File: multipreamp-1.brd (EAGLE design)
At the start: 100 x 50 mm, 138 parts, among them Q1 J201, Q2 J201, Q3 J201, Q4 J201, Q5 J201, Q6 J201, Q7 J201, Q8 2N5088

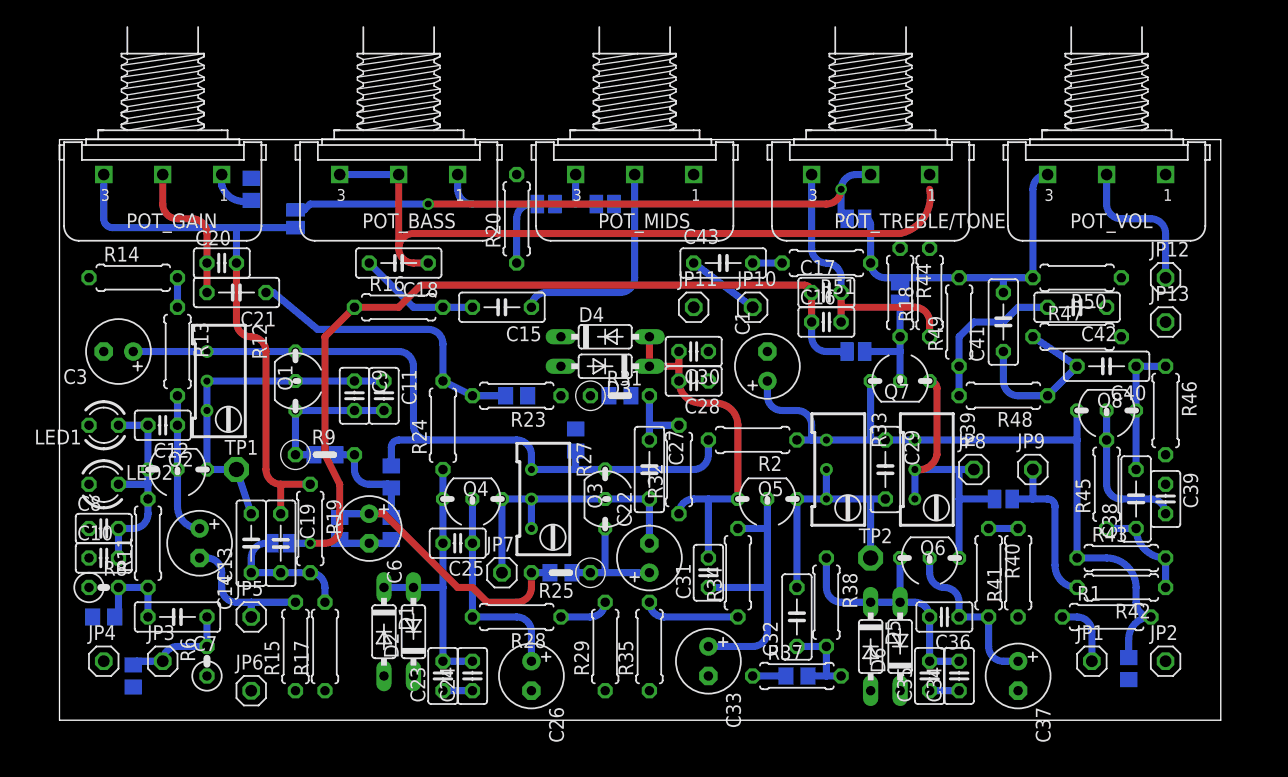
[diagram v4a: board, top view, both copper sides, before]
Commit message: Ajustes no layout - troca de encapsulamento dos trimpots
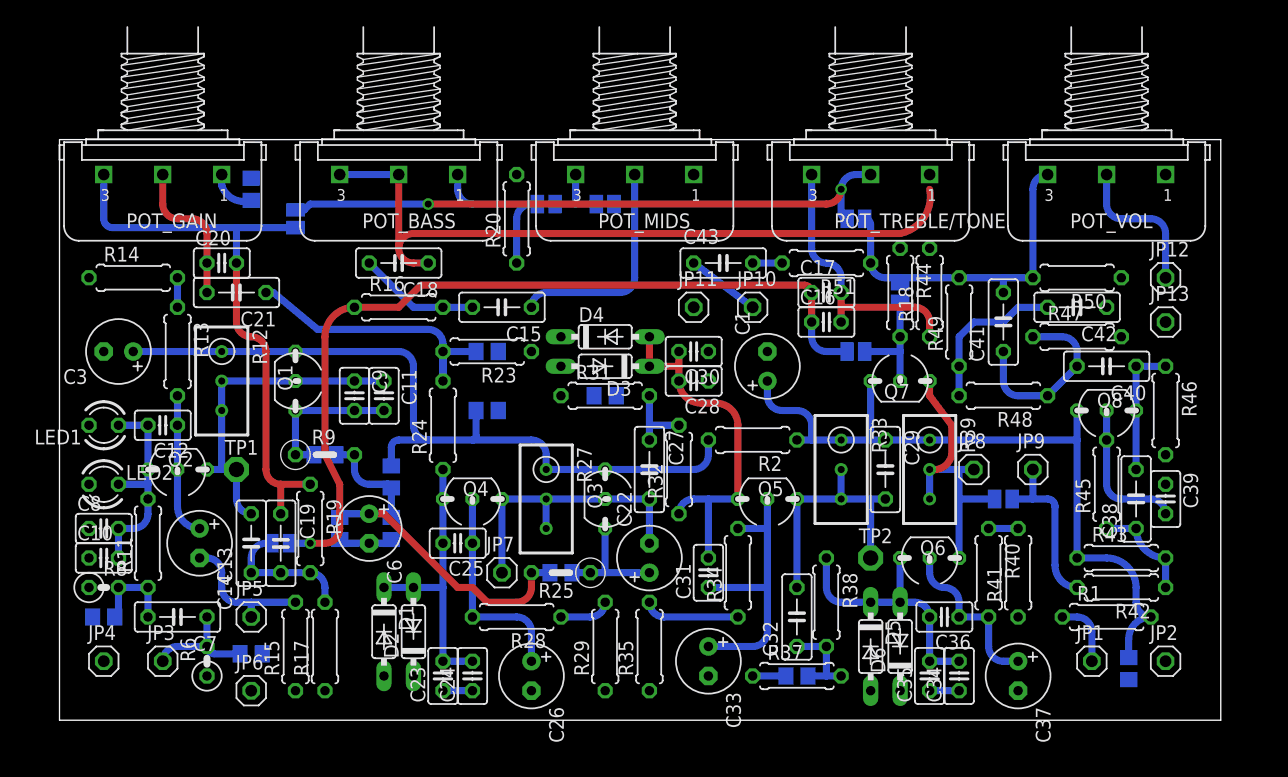
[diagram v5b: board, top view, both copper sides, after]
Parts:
- R12, R27, R33, R39: device rcl:RTRIM64W -> rcl:RTRIM3296W
- R31: device rcl:0207/5V -> rcl:0207/7
- moved R5 10.3 mm to (16.5, 5.71), turned to 0 degrees
- moved C4 8.03 mm to (36.8, 26.7), turned to 180 degrees
- moved R22 4.58 mm to (36.8, 31.8)
- moved R23 4.58 mm to (36.8, 31.8)
- moved R30 1.27 mm to (47.0, 27.9)
- moved R31 1.27 mm to (47.0, 27.9)
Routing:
- net V+: track 65.9 -> 67.0 mm
- net N$32: track 15.0 -> 16.1 mm
- net N$8: track 29.4 -> 28.5 mm
- net N$28: track 27.2 -> 26.3 mm

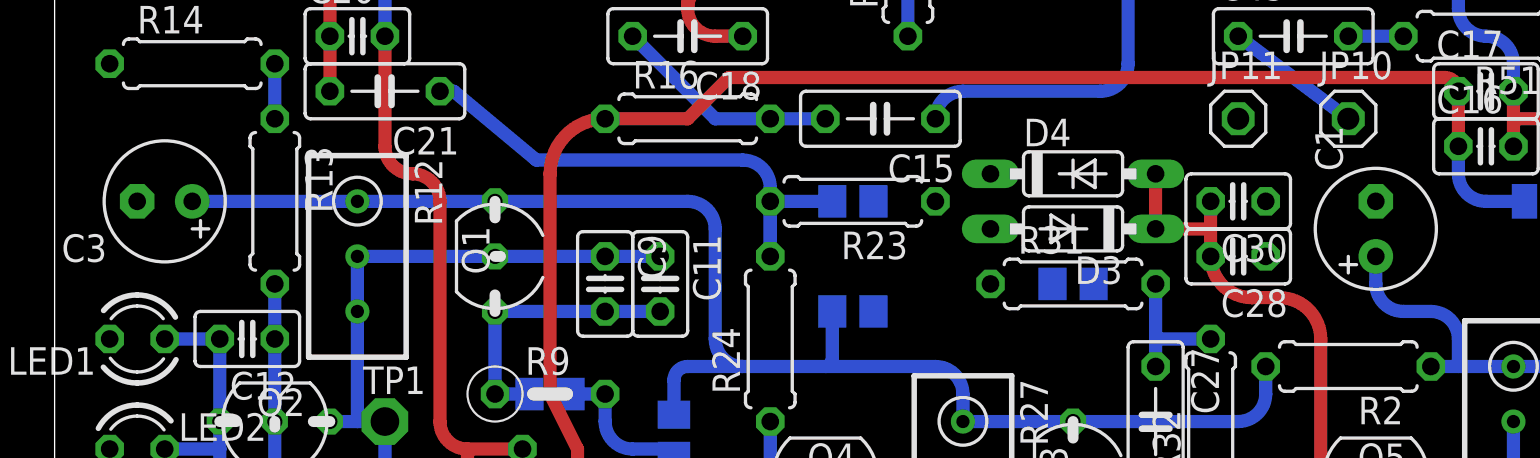
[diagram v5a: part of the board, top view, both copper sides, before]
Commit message: Ajustes no esquematico e adicao de capacitores de bypass
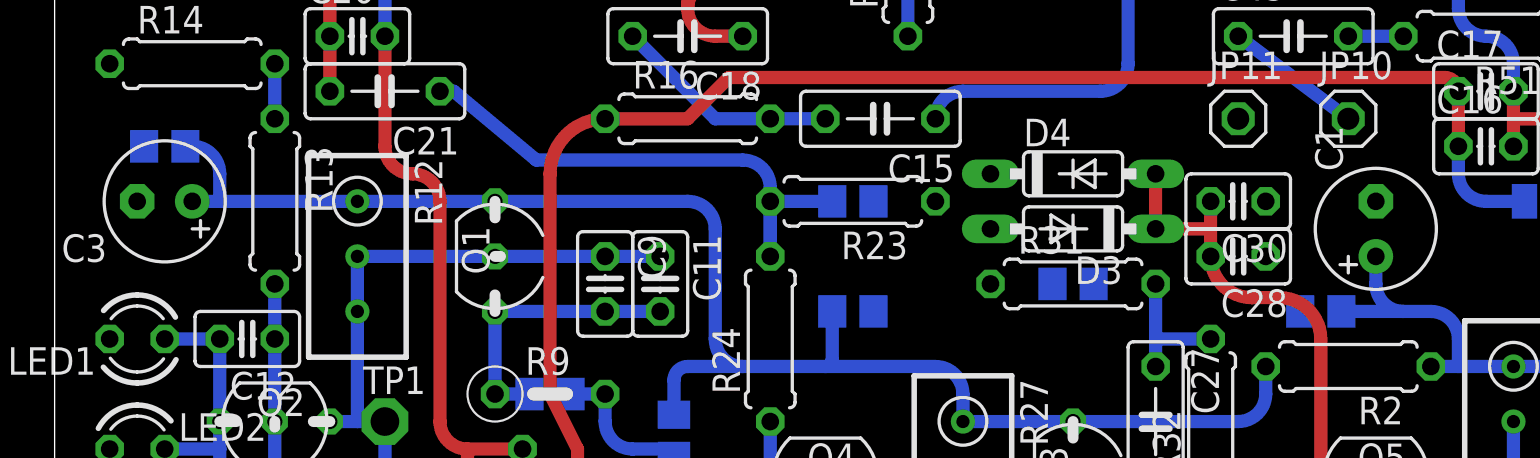
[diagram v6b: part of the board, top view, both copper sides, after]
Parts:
- added C44, C45: 100n SMD, rcl:C0805
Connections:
- removed net 9V_1: C1.+, C2.1, C29.1, Q7.3, Q8.1, R1.2, R2.1, R33.1, R39.1, R43.1
- removed net V+: C3.+, C4.1, Q1.3, Q3.3, R12.1, R2.2, R27.1, R3.1
- new net V+/1: C3.+, C4.1, C45.1, Q1.3, Q3.3, R12.1, R2.2, R27.1, R3.1
- new net V+/2: C1.+, C2.1, C29.1, C44.1, Q7.3, Q8.1, R1.2, R2.1, R33.1, R39.1, R43.1
- net GND: now also C44.2, C45.2
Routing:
- net V+/1: track 0.00 -> 70.3 mm
- net V+: track 67.0 -> 0.00 mm
- net V+/2: track 0.00 -> 65.7 mm
- net 9V_1: track 62.8 -> 0.00 mm
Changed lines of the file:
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@@
 <element name="SJ7" library="jumper" package="SJ" value="" x="72.39" y="36.83" rot="MR90"/>
 <element name="SJ8" library="jumper" package="SJ" value="" x="68.58" y="31.75" rot="MR0"/>
+<element name="C44" library="rcl" package="C0805" value="100n SMD" x="58.42" y="26.67" rot="MR0"/>
+<element name="C45" library="rcl" package="C0805" value="100n SMD" x="5.08" y="34.29" rot="MR0"/>
 </elements>
 <signals>
@@
 <contactref element="R17" pad="1"/>
 <contactref element="C3" pad="-"/>
+<contactref element="C44" pad="2"/>
+<contactref element="C45" pad="2"/>
 <wire x1="91.44" y1="38.1" x2="95.25" y2="46.99" width="0" layer="19" extent="1-1"/>
 <wire x1="90.17" y1="35.56" x2="91.44" y2="38.1" width="0" layer="19" extent="1-1"/>
@@
 <wire x1="2.54" y1="38.1" x2="3.81" y2="31.75" width="0" layer="19" extent="1-1"/>
 <wire x1="28.255" y1="15.24" x2="27.94" y2="3.81" width="0" layer="19" extent="16-16"/>
+<wire x1="4.13" y1="34.29" x2="3.81" y2="5.08" width="0" layer="19" extent="1-1"/>
 <wire x1="37.78" y1="26.67" x2="28.575" y2="15.56" width="0" layer="19" extent="16-16"/>
 <wire x1="37.78" y1="31.75" x2="37.78" y2="26.67" width="0" layer="19" extent="16-16"/>
@@
 <wire x1="55.88" y1="29.21" x2="46.04" y2="27.94" width="0" layer="19" extent="16-16"/>
 <wire x1="55.88" y1="31.75" x2="55.88" y2="29.21" width="0" layer="19" extent="1-1"/>
+<wire x1="57.47" y1="26.67" x2="55.88" y2="29.21" width="0" layer="19" extent="16-16"/>
 <wire x1="54.61" y1="35.56" x2="55.88" y2="31.75" width="0" layer="19" extent="1-1"/>
 <wire x1="60.96" y1="31.75" x2="55.88" y2="31.75" width="0" layer="19" extent="1-1"/>
@@
 <wire x1="77.47" y1="33.02" x2="77.47" y2="30.48" width="0.6096" layer="16"/>
 </signal>
-<signal name="V+">
+<signal name="V+/1">
 <contactref element="R27" pad="1"/>
 <contactref element="R12" pad="1"/>
@@
 <wire x1="54.61" y1="21.59" x2="55.88" y2="22.86" width="0.6096" layer="16" curve="90"/>
 <wire x1="55.88" y1="22.86" x2="55.88" y2="24.13" width="0.6096" layer="16"/>
-<wire x1="13.97" y1="31.75" x2="6.35" y2="31.75" width="0.6096" layer="16"/>
+<wire x1="13.97" y1="31.75" x2="7.62" y2="31.75" width="0.6096" layer="16"/>
+<wire x1="7.62" y1="31.75" x2="6.35" y2="31.75" width="0.6096" layer="16"/>
 <wire x1="35.88" y1="26.67" x2="35.88" y2="24.45" width="0.6096" layer="16"/>
 <wire x1="35.88" y1="24.45" x2="35.56" y2="24.13" width="0.6096" layer="16" curve="-90"/>
+<contactref element="C45" pad="1"/>
+<wire x1="6.03" y1="34.29" x2="6.35" y2="34.29" width="0.6096" layer="16"/>
+<wire x1="6.35" y1="34.29" x2="7.62" y2="33.02" width="0.6096" layer="16" curve="-90"/>
+<wire x1="7.62" y1="33.02" x2="7.62" y2="31.75" width="0.6096" layer="16"/>
 </signal>
 <signal name="N$35">
@@
 <wire x1="41.91" y1="36.83" x2="40.64" y2="35.56" width="0.6096" layer="16" curve="90"/>
 </signal>
-<signal name="9V_1">
+<signal name="V+/2">
 <contactref element="C2" pad="1"/>
 <contactref element="C1" pad="+"/>
@@
 <wire x1="64.77" y1="25.4" x2="64.77" y2="24.13" width="0.6096" layer="16"/>
 <wire x1="69.85" y1="29.21" x2="69.85" y2="24.13" width="0.6096" layer="16"/>
+<contactref element="C44" pad="1"/>
+<wire x1="59.37" y1="26.67" x2="62.23" y2="26.67" width="0.6096" layer="16"/>
 </signal>
 <signal name="N$44">

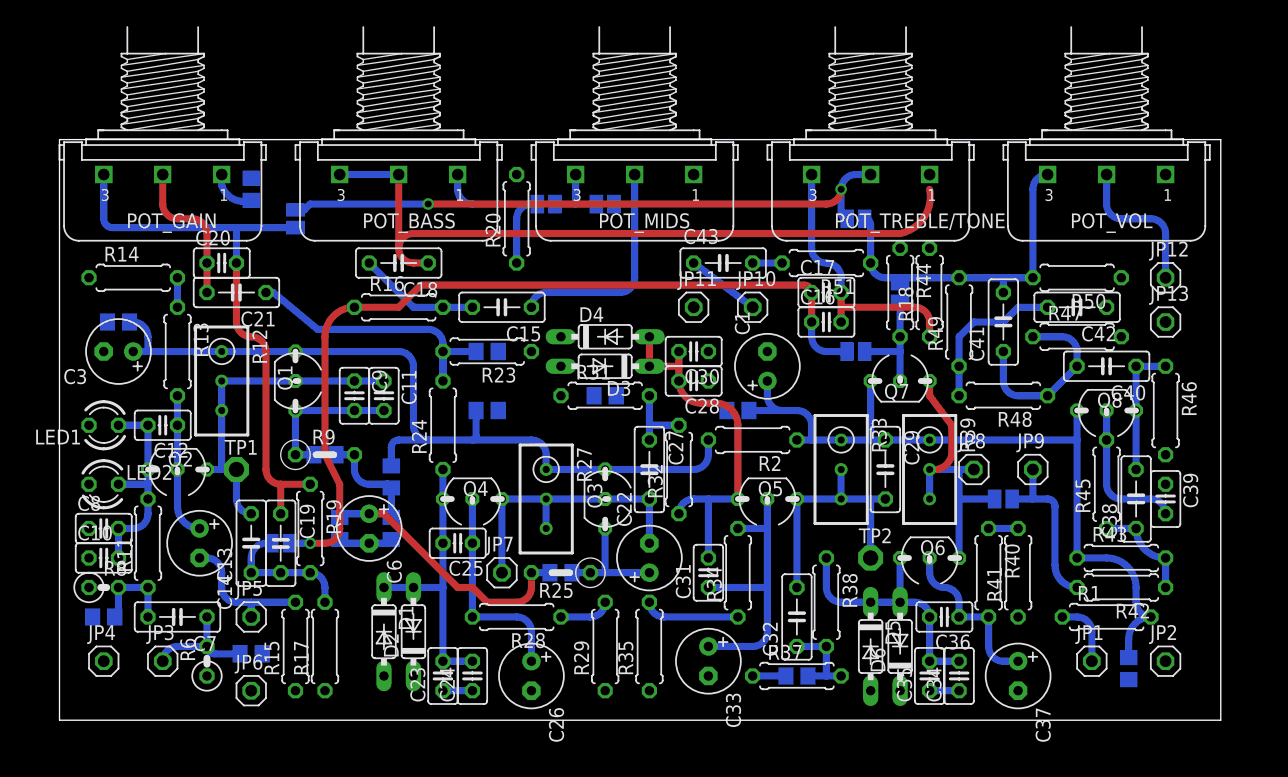
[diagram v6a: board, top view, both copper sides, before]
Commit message: Ajustes no layout e criacao do plano de terra DRC executado, sem erros
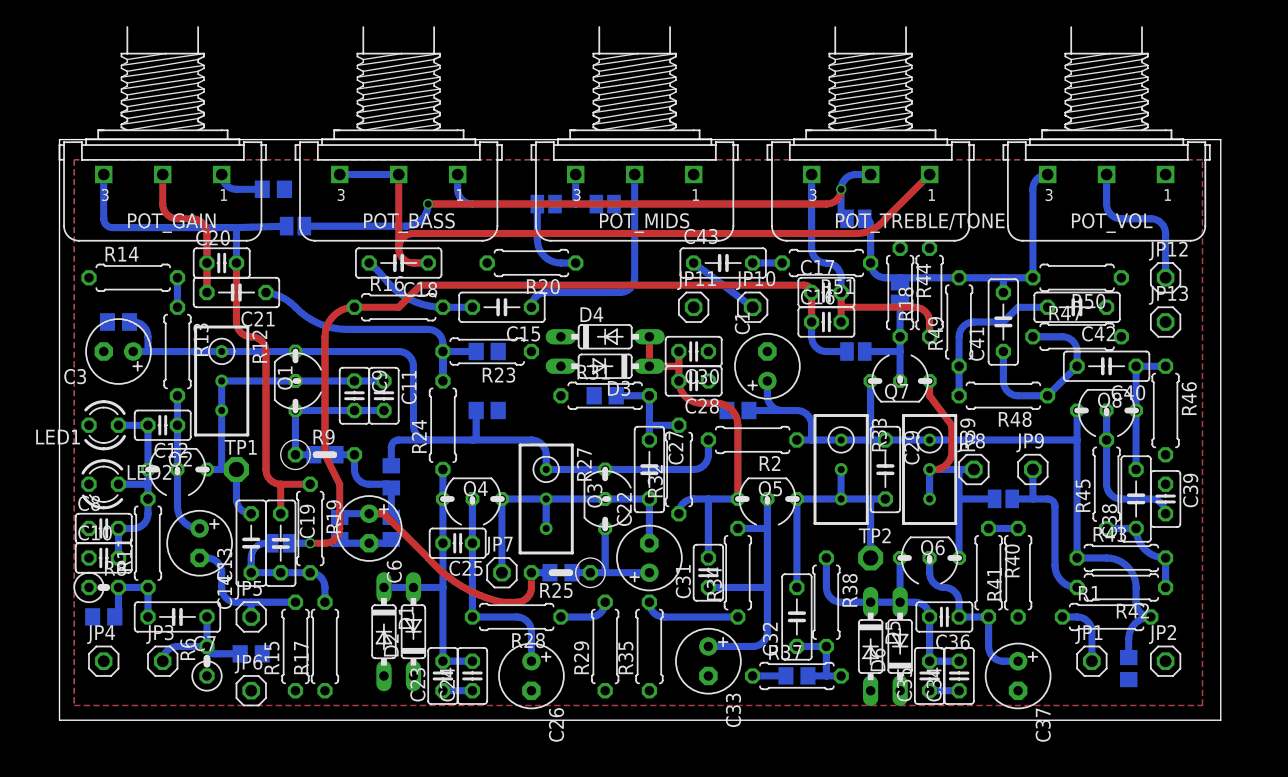
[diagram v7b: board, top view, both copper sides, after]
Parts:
- moved R20 4.02 mm to (40.6, 39.4), turned to 180 degrees
- moved R21 1.90 mm to (18.4, 45.7), turned to 0 degrees
- moved SJ4 0.63 mm to (20.3, 42.5), turned to 0 degrees
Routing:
- net N$18: track 6.35 -> 9.21 mm
- net N$43: track 14.8 -> 15.8 mm
- net N$11: track 49.4 -> 48.6 mm
- net VCC/2: track 34.5 -> 33.9 mm
- added copper zone on layer 1, net GND
- added copper zone on layer 16, net GND

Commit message: Troca do potenciometro por modelo com layers corretos para silkagem na PCB Ajustes no layout
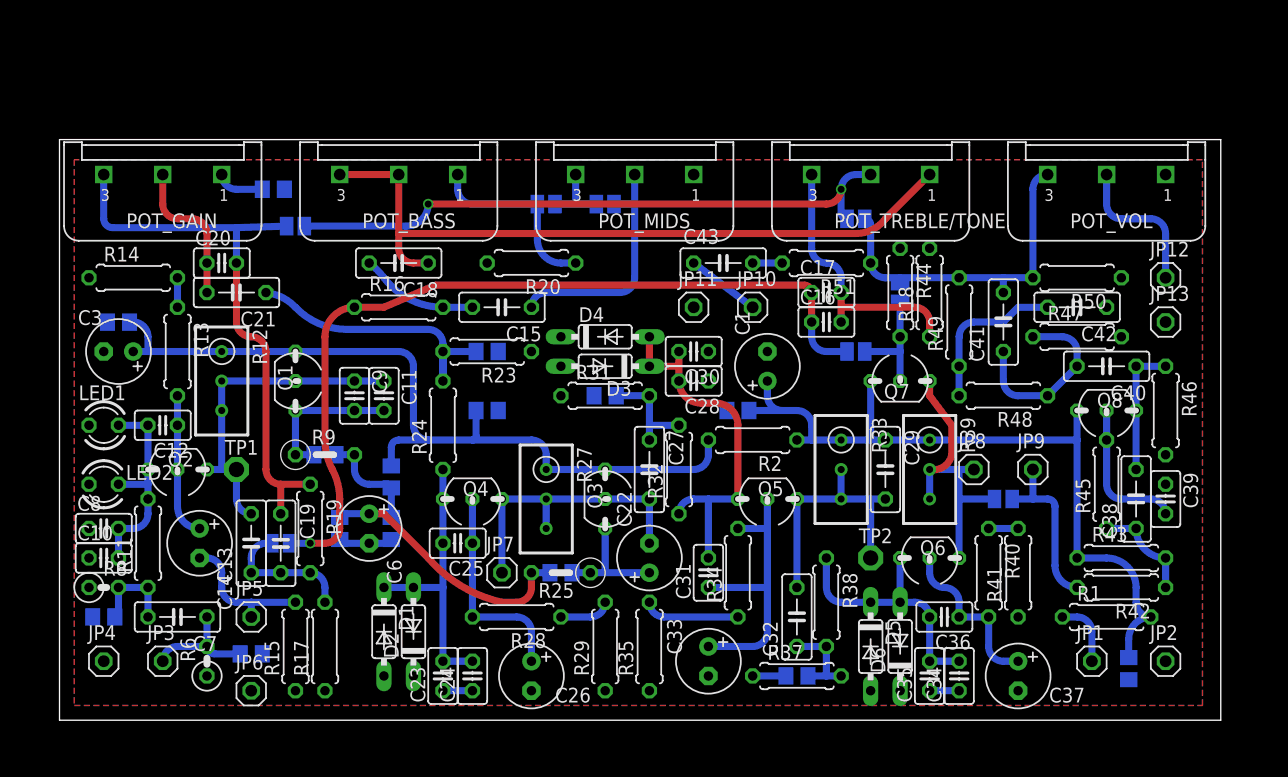
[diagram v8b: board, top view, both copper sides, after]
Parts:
- POT_BASS, POT_GAIN, POT_MIDS, POT_TREBLE/TONE, POT_VOL: device gm-pots:16MM-PCB-MOUNT -> PATSKO:16MM-PCB-MOUNT
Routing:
- net TONE_IN: track 73.1 -> 72.5 mm
- net TONE/TREBLE_1: track 62.6 -> 62.1 mm
